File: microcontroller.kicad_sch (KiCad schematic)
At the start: 13 parts, among them SW1 Boot Switch, SW2 System Reset, U2 STM32F401RETx

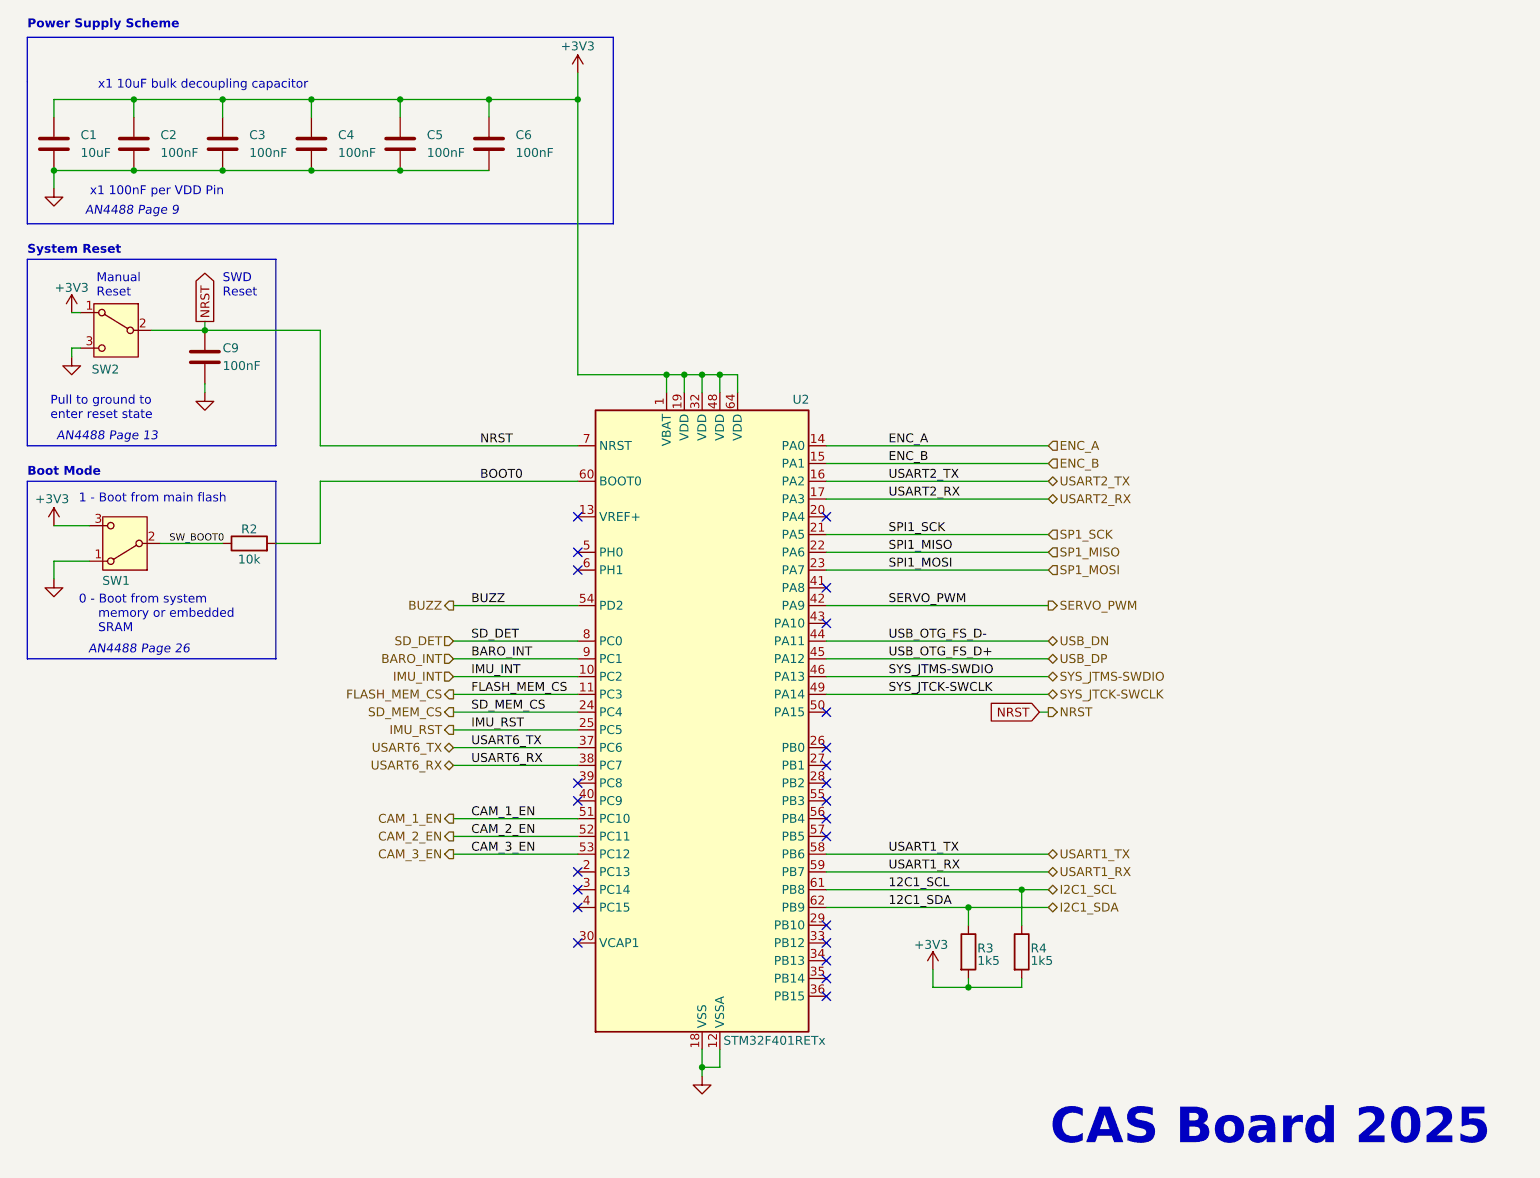
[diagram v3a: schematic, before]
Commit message: Initial layout for PCB components, updated README with images. Removed some test points and headers from final layout. Pending addition of buzzer. Pending additional power testing and pending routing.
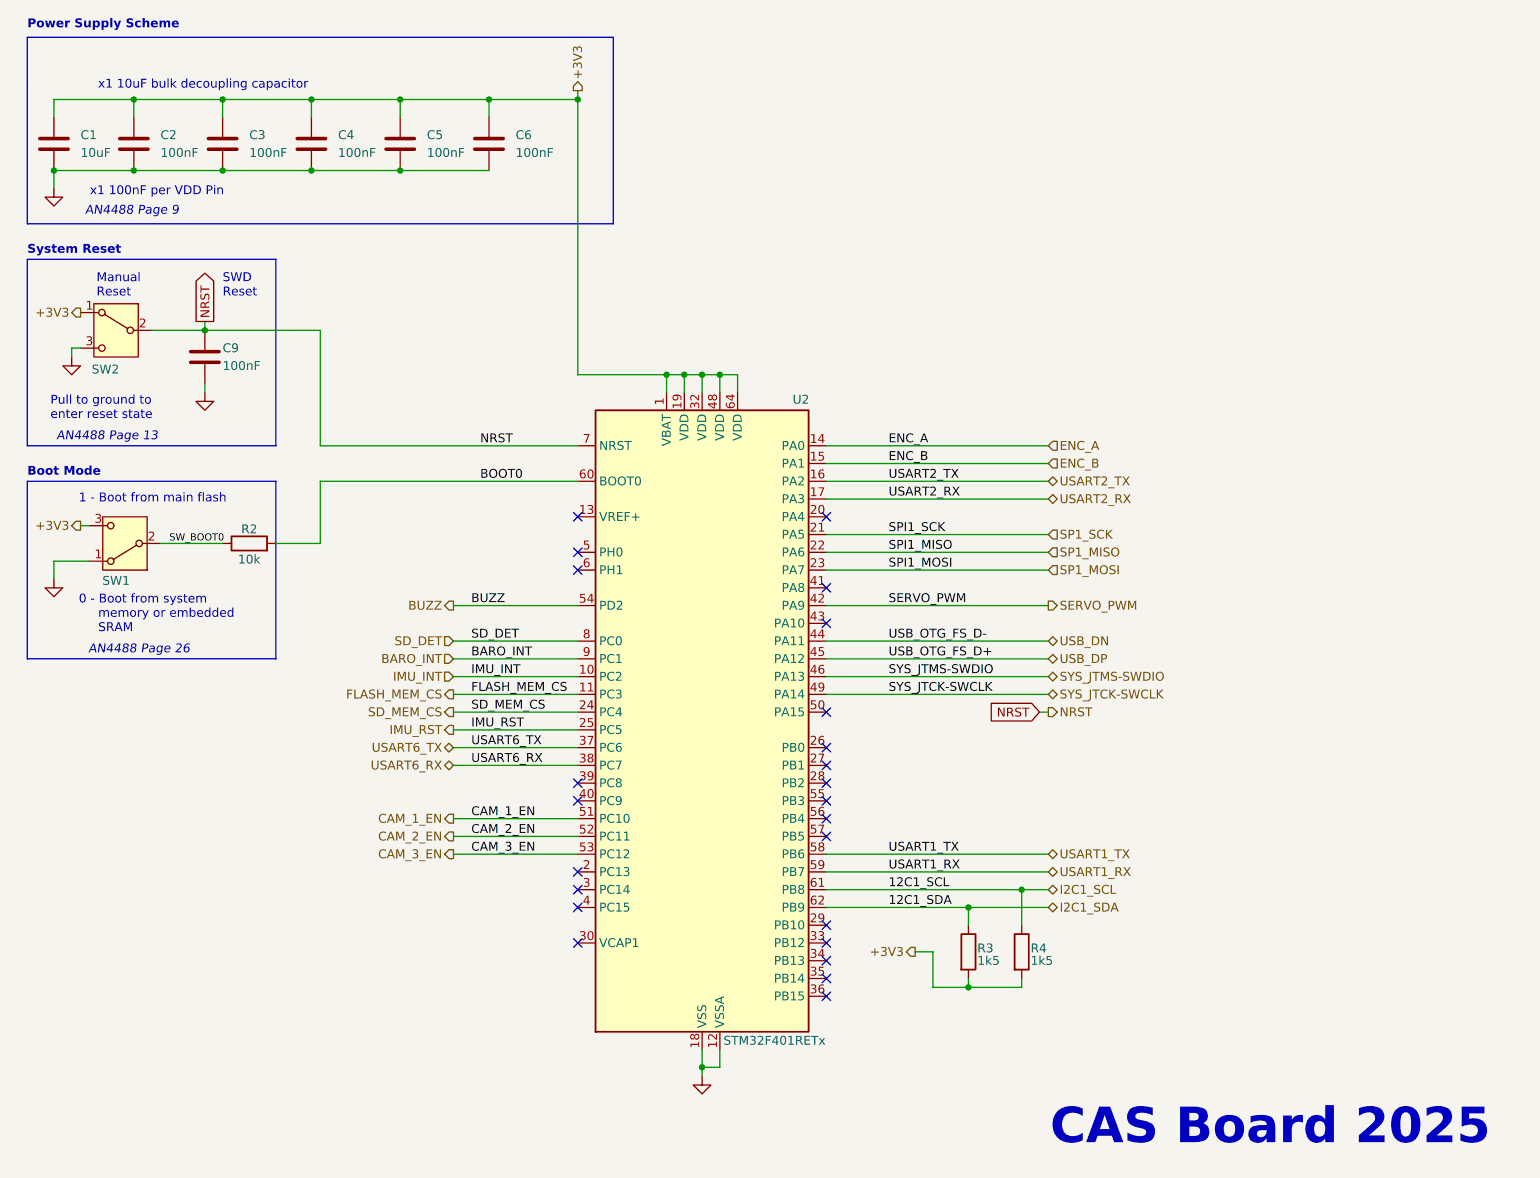
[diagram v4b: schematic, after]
